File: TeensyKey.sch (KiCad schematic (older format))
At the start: 1 part

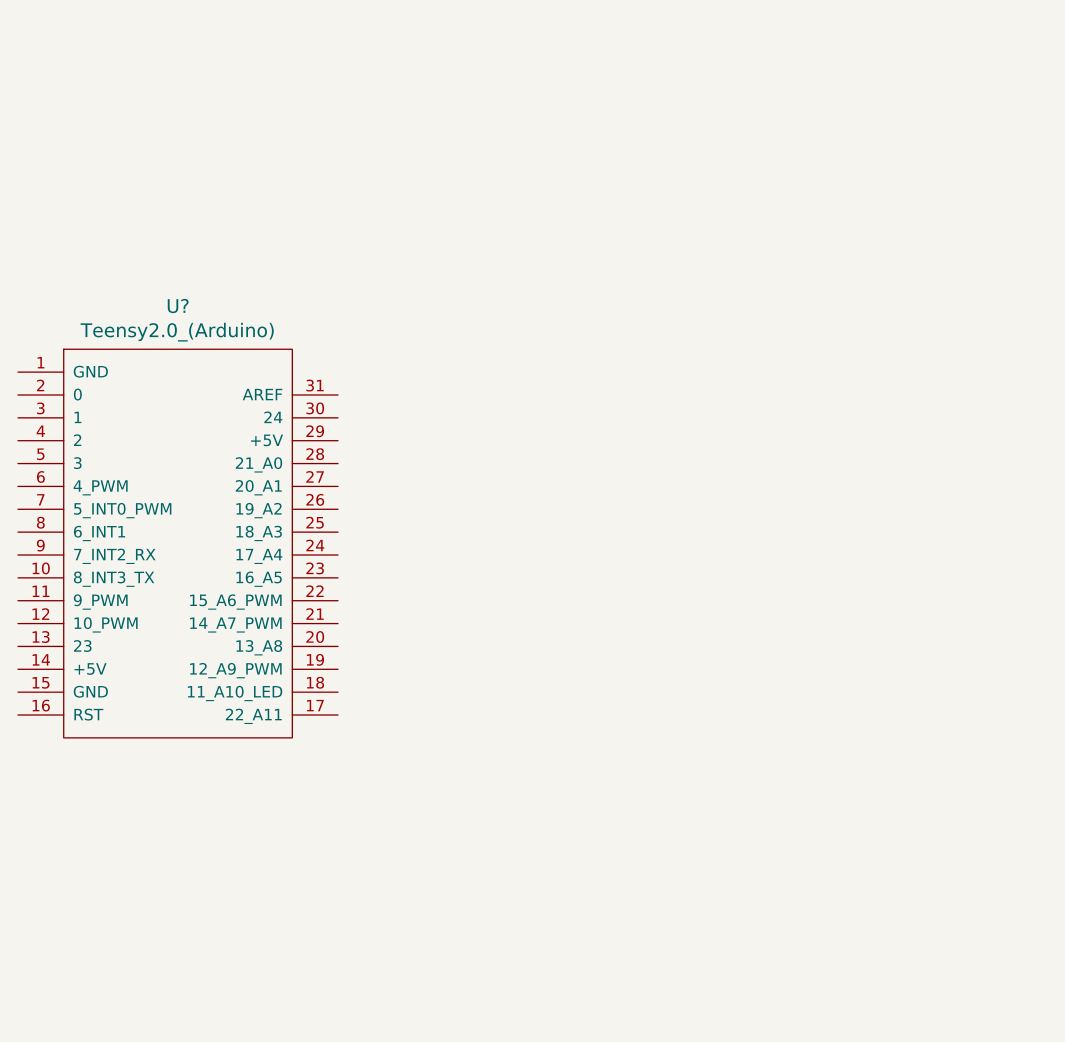
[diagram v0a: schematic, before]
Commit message: adding items to schematic
switched component & footprint references to be
project-relative using KIPRJMOD env variable
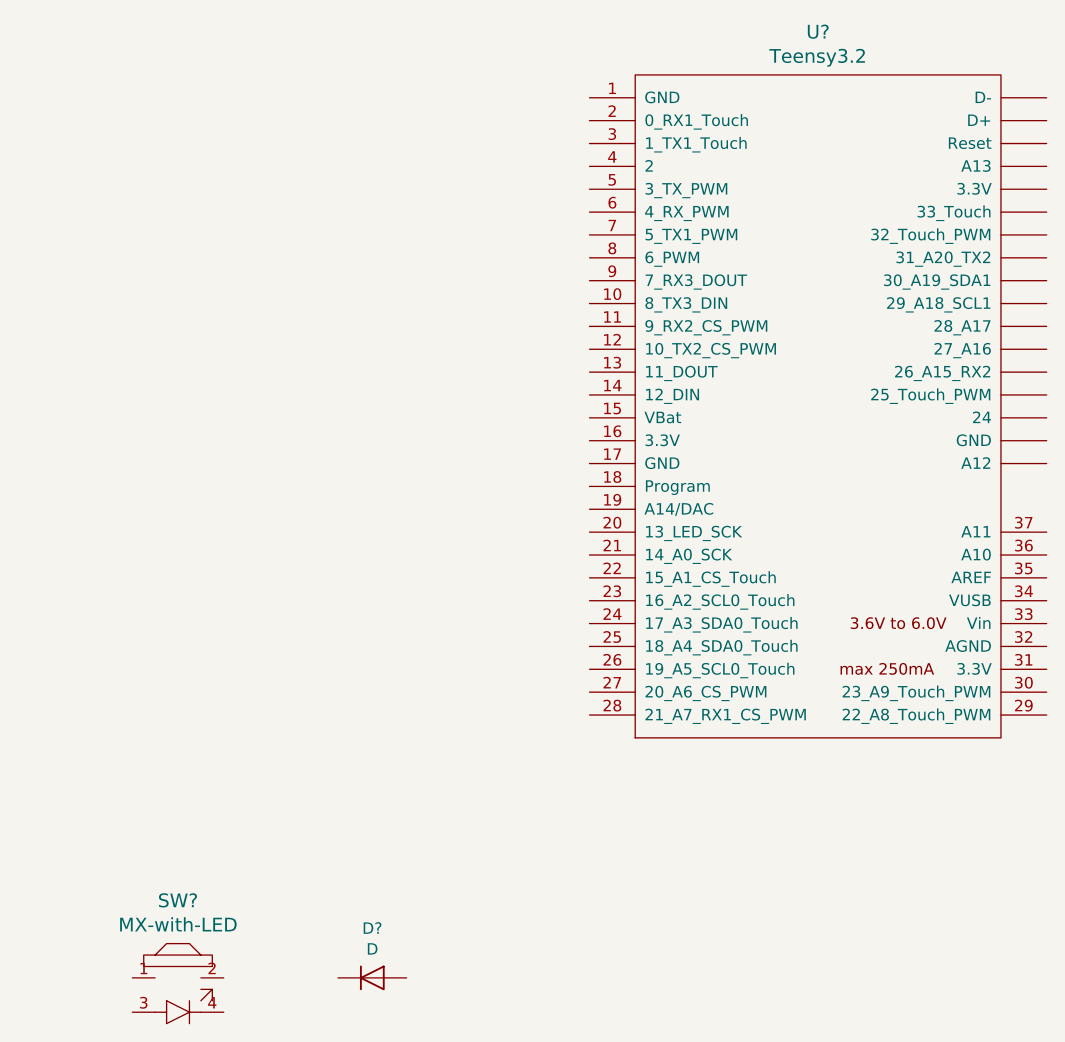
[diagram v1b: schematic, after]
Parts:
- removed U?: Teensy2.0_(Arduino), symbol teensy:Teensy2.0_(Arduino)
- added D?: D, symbol Device:D
- added SW?: MX-with-LED, symbol keebio:MX-with-LED
- added U?: Teensy3.2, symbol teensy:Teensy3.2
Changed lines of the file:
@@
 $EndDescr
 $Comp
-L teensy:Teensy2.0_(Arduino) U?
-U 1 1 5DEF3831
-P 3950 3350
-F 0 "U?" H 3950 4387 60  0000 C CNN
-F 1 "Teensy2.0_(Arduino)" H 3950 4281 60  0000 C CNN
-F 2 "" H 4050 2300 60  0000 C CNN
-F 3 "" H 4050 2300 60  0000 C CNN
-	1    3950 3350
+L keebio:MX-with-LED SW?
+U 1 1 5DF11BDF
+P 3950 5250
+F 0 "SW?" H 3950 5587 60  0000 C CNN
+F 1 "MX-with-LED" H 3950 5481 60  0000 C CNN
+F 2 "" H 3950 5250 60  0001 C CNN
+F 3 "" H 3950 5250 60  0001 C CNN
+	1    3950 5250
 	1    0    0    -1
 $EndComp
+$Comp
+L Device:D D?
+U 1 1 5DF13768
+P 4800 5250
+F 0 "D?" H 4800 5466 50  0000 C CNN
+F 1 "D" H 4800 5375 50  0000 C CNN
+F 2 "" H 4800 5250 50  0001 C CNN
+F 3 "~" H 4800 5250 50  0001 C CNN
+	1    4800 5250
+	1    0    0    -1
+$EndComp
+$Comp
+L teensy:Teensy3.2 U?
+U 1 1 5DF14A40
+P 6750 2750
+F 0 "U?" H 6750 4387 60  0000 C CNN
+F 1 "Teensy3.2" H 6750 4281 60  0000 C CNN
+F 2 "" H 6750 2000 60  0000 C CNN
+F 3 "" H 6750 2000 60  0000 C CNN
+	1    6750 2750
+	1    0    0    -1
+$EndComp

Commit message: switched footprint to my version
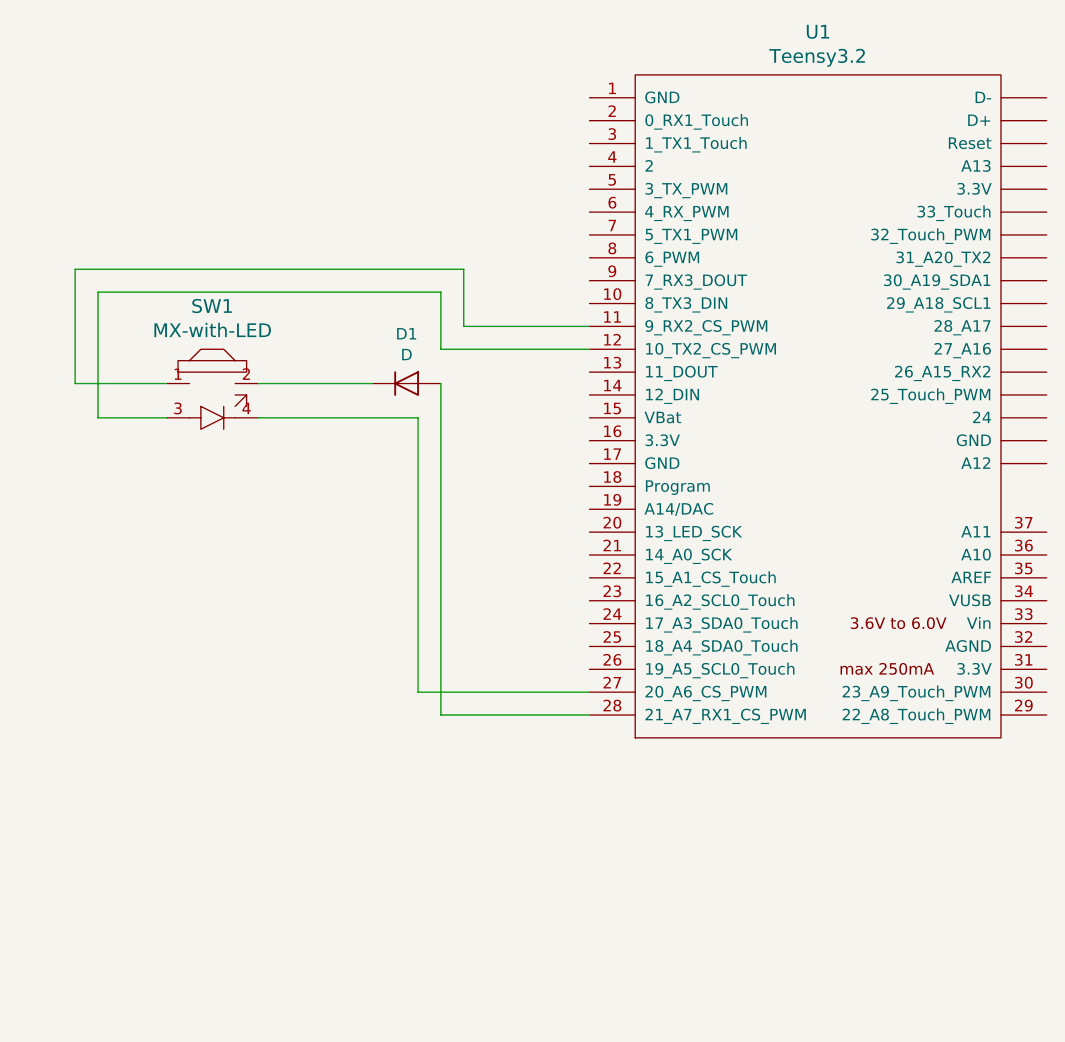
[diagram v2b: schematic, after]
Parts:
- D1: renamed from D?; footprint (none) -> Diodes_THT:D_DO-35_SOD27_P7.62mm_Horizontal
- SW1: renamed from SW?; footprint (none) -> keebio:MX-Alps-Choc-1U
- U1: renamed from U?; footprint (none) -> chillpizza:Teensy30_31_32_LC_smt_combi
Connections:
- net at SW1.1: now also U1.11 (9_RX2_CS_PWM)
- net at SW1.2: now also D1.1 (K)
- net at SW1.3: now also U1.12 (10_TX2_CS_PWM)
- net at SW1.4: now also U1.27 (20_A6_CS_PWM)
- net at D1.2 (A): now also U1.28 (21_A7_RX1_CS_PWM)
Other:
- moved on the sheet: D1, SW1
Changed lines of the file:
@@
 $EndDescr
 $Comp
-L keebio:MX-with-LED SW?
+L keebio:MX-with-LED SW1
 U 1 1 5DF11BDF
-P 3950 5250
-F 0 "SW?" H 3950 5587 60  0000 C CNN
-F 1 "MX-with-LED" H 3950 5481 60  0000 C CNN
-F 2 "" H 3950 5250 60  0001 C CNN
-F 3 "" H 3950 5250 60  0001 C CNN
-	1    3950 5250
+P 4100 2650
+F 0 "SW1" H 4100 2987 60  0000 C CNN
+F 1 "MX-with-LED" H 4100 2881 60  0000 C CNN
+F 2 "keebio:MX-Alps-Choc-1U" H 4100 2650 60  0001 C CNN
+F 3 "" H 4100 2650 60  0001 C CNN
+	1    4100 2650
 	1    0    0    -1
 $EndComp
 $Comp
-L Device:D D?
+L Device:D D1
 U 1 1 5DF13768
-P 4800 5250
-F 0 "D?" H 4800 5466 50  0000 C CNN
-F 1 "D" H 4800 5375 50  0000 C CNN
-F 2 "" H 4800 5250 50  0001 C CNN
-F 3 "~" H 4800 5250 50  0001 C CNN
-	1    4800 5250
+P 4950 2650
+F 0 "D1" H 4950 2866 50  0000 C CNN
+F 1 "D" H 4950 2775 50  0000 C CNN
+F 2 "Diodes_THT:D_DO-35_SOD27_P7.62mm_Horizontal" H 4950 2650 50  0001 C CNN
+F 3 "~" H 4950 2650 50  0001 C CNN
+	1    4950 2650
 	1    0    0    -1
 $EndComp
 $Comp
-L teensy:Teensy3.2 U?
+L teensy:Teensy3.2 U1
 U 1 1 5DF14A40
 P 6750 2750
-F 0 "U?" H 6750 4387 60  0000 C CNN
+F 0 "U1" H 6750 4387 60  0000 C CNN
 F 1 "Teensy3.2" H 6750 4281 60  0000 C CNN
-F 2 "" H 6750 2000 60  0000 C CNN
+F 2 "chillpizza:Teensy30_31_32_LC_smt_combi" H 6750 2000 60  0001 C CNN
 F 3 "" H 6750 2000 60  0000 C CNN
 	1    6750 2750
 	1    0    0    -1
 $EndComp
+Wire Wire Line
+	4800 2650 4300 2650
+Wire Wire Line
+	3900 2650 3500 2650
+Wire Wire Line
+	3500 2650 3500 2150
+Wire Wire Line
+	3500 2150 5200 2150
+Wire Wire Line
+	5200 2150 5200 2400
+Wire Wire Line
+	5200 2400 5750 2400
+Wire Wire Line
+	5100 4100 5750 4100
+Wire Wire Line
+	5100 2650 5100 4100
+Wire Wire Line
+	5750 4000 5000 4000
+Wire Wire Line
+	5000 4000 5000 2800
+Wire Wire Line
+	5000 2800 4300 2800
+Wire Wire Line
+	3900 2800 3600 2800
+Wire Wire Line
+	3600 2800 3600 2250
+Wire Wire Line
+	3600 2250 5100 2250
+Wire Wire Line
+	5100 2250 5100 2500
+Wire Wire Line
+	5100 2500 5750 2500
 $EndSCHEMATC
